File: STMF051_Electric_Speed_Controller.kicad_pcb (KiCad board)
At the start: 4 copper layers, 46 x 47 mm, 164 parts, among them J1 Conn_01x03_Pin, J2 Conn_01x03_Pin, J3 Conn_01x03_Pin, J4 Conn_01x03_Pin, J5 Conn_01x03_Pin, J6 Conn_01x03_Pin, Q1 TPH3R704PL,L1Q, Q10 TPH3R704PL,L1Q, Q11 TPH3R704PL,L1Q, Q12 TPH3R704PL,L1Q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

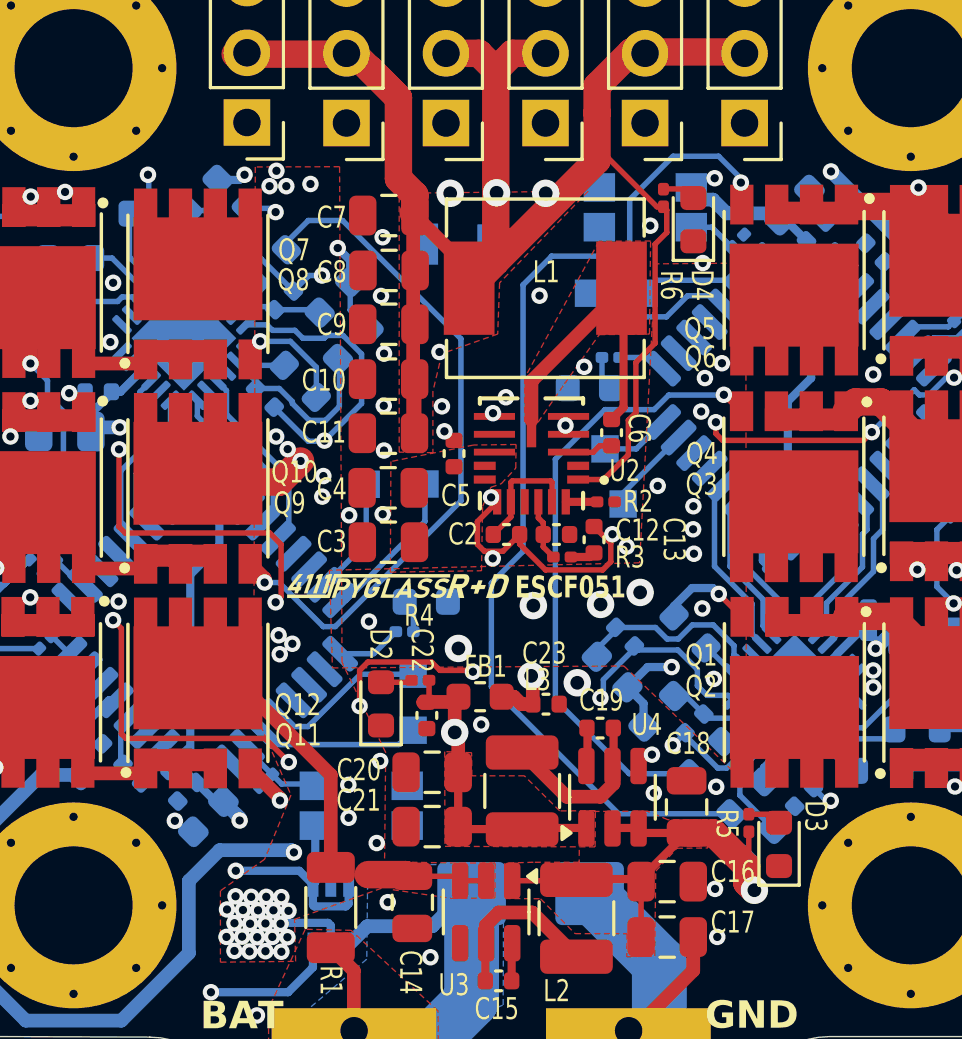
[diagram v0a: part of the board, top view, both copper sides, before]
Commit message: change charge diodes footprint from plain 0603 to X3-TSN1608-2 which has asymetric pads
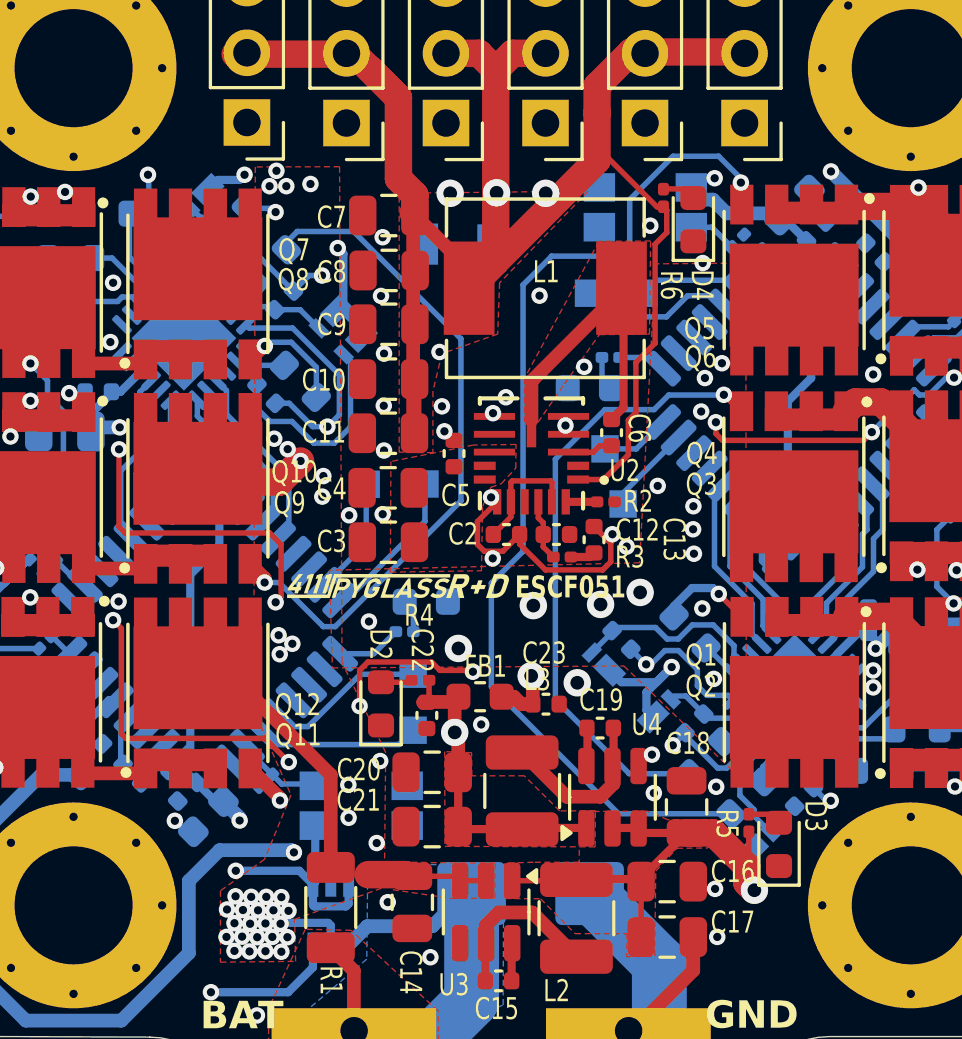
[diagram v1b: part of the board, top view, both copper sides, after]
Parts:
- D10, D11, D12, D7, D8, D9: value SDM4A40EP3-7B -> SDT4U40EP3-7B; footprint Diode_SMD:D_0603_1608Metric -> ProjectLibrary:X3-TSN1608-2
- moved D11 0.71 mm to (94.1, 94.8)
- moved D7 0.40 mm to (104.1, 107.5)
- moved C40 0.18 mm to (104.7, 106.6)
- moved C43 0.15 mm to (91.8, 97.6)
- moved D10 0.11 mm to (95.0, 95.7)
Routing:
- net PHASE1_B: track 40.3 -> 37.8 mm
- net /FET Driver/VB1_B: track 6.82 -> 8.96 mm
- net +5V: track 129.5 -> 131.5 mm
